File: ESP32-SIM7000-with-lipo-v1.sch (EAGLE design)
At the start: 72 parts, among them IC2 TXB0104, Q1 BSS138L, Q2 BSS138L, Q3 9013, Q5 9013, U3 ESP-WROOM-32, U4 MCP73831T-2ACI/OT, X1 LTE-uFL

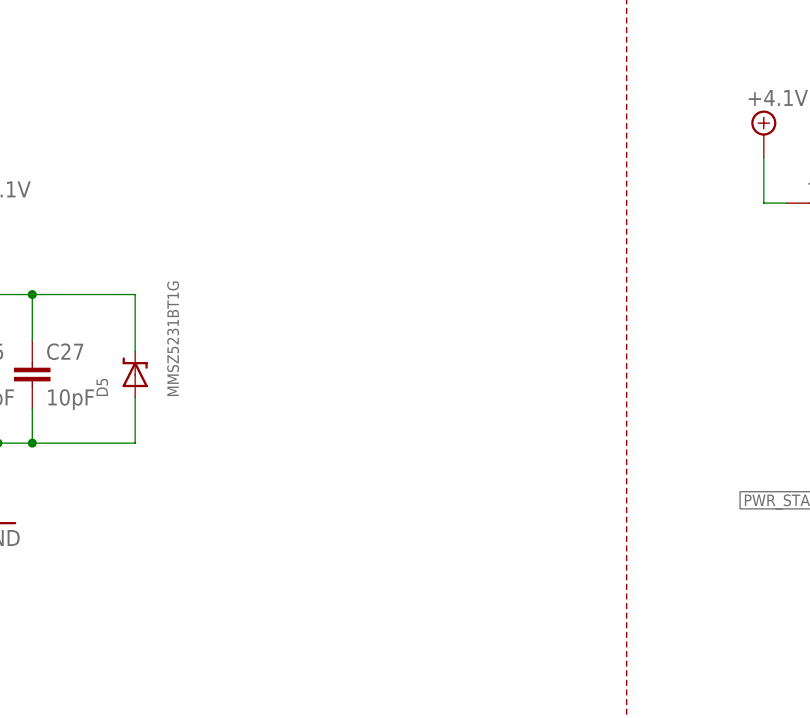
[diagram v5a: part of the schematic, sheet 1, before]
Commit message: Adds power caps
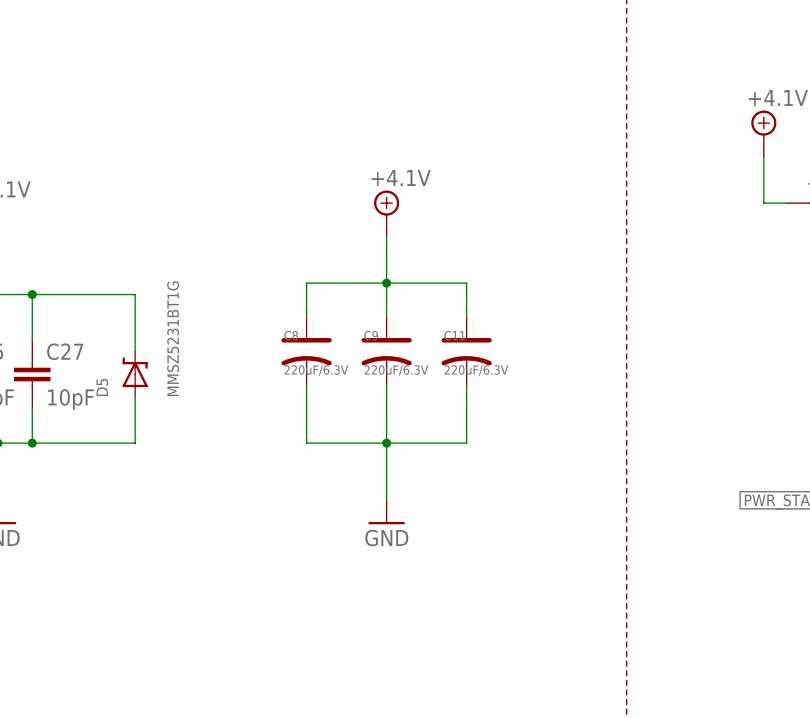
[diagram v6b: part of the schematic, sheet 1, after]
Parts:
- added C11, C8, C9: 220uF/6.3V, discrete:006-CAP_AVX_B
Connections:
- net +4.1V: now also C11.+, C8.+, C9.+
- net GND: now also C11.-, C8.-, C9.-
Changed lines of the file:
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@@
 <setting verticaltext="up"/>
 </settings>
-<grid distance="0.1" unitdist="inch" unit="inch" style="lines" multiple="1" display="no" altdistance="0.01" altunitdist="inch" altunit="inch"/>
+<grid distance="0.05" unitdist="inch" unit="inch" style="lines" multiple="1" display="no" altdistance="0.01" altunitdist="inch" altunit="inch"/>
 <layers>
 <layer number="1" name="Top" color="4" fill="1" visible="yes" active="no"/>
@@
 <part name="GND47" library="SparkFun" deviceset="GND" device=""/>
 <part name="SUPPLY9" library="supply2" library_urn="urn:adsk.eagle:library:372" deviceset="+4.1V" device=""/>
+<part name="C8" library="discrete" deviceset="006-CAP*" device="_AVX_B" value="220uF/6.3V"/>
+<part name="GND42" library="SparkFun" deviceset="GND" device=""/>
+<part name="C9" library="discrete" deviceset="006-CAP*" device="_AVX_B" value="220uF/6.3V"/>
+<part name="C11" library="discrete" deviceset="006-CAP*" device="_AVX_B" value="220uF/6.3V"/>
+<part name="SUPPLY11" library="supply2" library_urn="urn:adsk.eagle:library:372" deviceset="+4.1V" device=""/>
 </parts>
 <sheets>
@@
 <instance part="SUPPLY9" gate="P" x="66.04" y="60.96">
 <attribute name="VALUE" x="64.135" y="64.135" size="1.778" layer="96"/>
+</instance>
+<instance part="C8" gate="C" x="101.6" y="46.99" smashed="yes" rot="R270">
+<attribute name="NAME" x="99.06" y="48.26" size="1.016" layer="95" ratio="10"/>
+<attribute name="VALUE" x="99.06" y="44.45" size="1.016" layer="96" ratio="10"/>
+</instance>
+<instance part="GND42" gate="1" x="110.49" y="27.94" rot="MR0"/>
+<instance part="C9" gate="C" x="110.49" y="46.99" smashed="yes" rot="R270">
+<attribute name="NAME" x="107.95" y="48.26" size="1.016" layer="95" ratio="10"/>
+<attribute name="VALUE" x="107.95" y="44.45" size="1.016" layer="96" ratio="10"/>
+</instance>
+<instance part="C11" gate="C" x="119.38" y="46.99" smashed="yes" rot="R270">
+<attribute name="NAME" x="116.84" y="48.26" size="1.016" layer="95" ratio="10"/>
+<attribute name="VALUE" x="116.84" y="44.45" size="1.016" layer="96" ratio="10"/>
+</instance>
+<instance part="SUPPLY11" gate="P" x="110.49" y="62.23">
+<attribute name="VALUE" x="108.585" y="65.405" size="1.778" layer="96"/>
 </instance>
 </instances>
@@
 <junction x="67.31" y="36.83"/>
 </segment>
+<segment>
+<pinref part="C8" gate="C" pin="-"/>
+<wire x1="101.6" y1="43.18" x2="101.6" y2="36.83" width="0.1524" layer="91"/>
+<pinref part="C11" gate="C" pin="-"/>
+<wire x1="101.6" y1="36.83" x2="110.49" y2="36.83" width="0.1524" layer="91"/>
+<wire x1="110.49" y1="36.83" x2="119.38" y2="36.83" width="0.1524" layer="91"/>
+<wire x1="119.38" y1="36.83" x2="119.38" y2="43.18" width="0.1524" layer="91"/>
+<pinref part="C9" gate="C" pin="-"/>
+<wire x1="110.49" y1="43.18" x2="110.49" y2="36.83" width="0.1524" layer="91"/>
+<junction x="110.49" y="36.83"/>
+<pinref part="GND42" gate="1" pin="GND"/>
+<wire x1="110.49" y1="30.48" x2="110.49" y2="36.83" width="0.1524" layer="91"/>
+</segment>
 </net>
 <net name="1.8V" class="0">
@@
 <pinref part="SUPPLY9" gate="P" pin="+4.1V"/>
 </segment>
-</net>
+<segment>
+<pinref part="C8" gate="C" pin="+"/>
+<wire x1="101.6" y1="50.8" x2="101.6" y2="54.61" width="0.1524" layer="91"/>
+<wire x1="101.6" y1="54.61" x2="110.49" y2="54.61" width="0.1524" layer="91"/>
+<wire x1="110.49" y1="54.61" x2="119.38" y2="54.61" width="0.1524" layer="91"/>
+<wire x1="119.38" y1="54.61" x2="119.38" y2="50.8" width="0.1524" layer="91"/>
+<pinref part="C11" gate="C" pin="+"/>
+<pinref part="C9" gate="C" pin="+"/>
+<wire x1="110.49" y1="50.8" x2="110.49" y2="54.61" width="0.1524" layer="91"/>
+<junction x="110.49" y="54.61"/>
+<pinref part="SUPPLY11" gate="P" pin="+4.1V"/>
+<wire x1="110.49" y1="59.69" x2="110.49" y2="54.61" width="0.1524" layer="91"/>
+</segment>
+</net>

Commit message: change caps package
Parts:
- C11, C8, C9: device discrete:006-CAP_AVX_B -> discrete:006-CAP_AVX_C
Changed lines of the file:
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@@
 <part name="GND47" library="SparkFun" deviceset="GND" device=""/>
 <part name="SUPPLY9" library="supply2" library_urn="urn:adsk.eagle:library:372" deviceset="+4.1V" device=""/>
-<part name="C8" library="discrete" deviceset="006-CAP*" device="_AVX_B" value="220uF/6.3V"/>
+<part name="C8" library="discrete" deviceset="006-CAP*" device="_AVX_C" value="220uF/6.3V"/>
 <part name="GND42" library="SparkFun" deviceset="GND" device=""/>
-<part name="C9" library="discrete" deviceset="006-CAP*" device="_AVX_B" value="220uF/6.3V"/>
-<part name="C11" library="discrete" deviceset="006-CAP*" device="_AVX_B" value="220uF/6.3V"/>
+<part name="C9" library="discrete" deviceset="006-CAP*" device="_AVX_C" value="220uF/6.3V"/>
+<part name="C11" library="discrete" deviceset="006-CAP*" device="_AVX_C" value="220uF/6.3V"/>
 <part name="SUPPLY11" library="supply2" library_urn="urn:adsk.eagle:library:372" deviceset="+4.1V" device=""/>
 </parts>
